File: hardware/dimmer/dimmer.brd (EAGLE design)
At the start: 112.1 x 40.6 mm, 34 parts, among them IC1 MEGA328PU, IC2 RFM12, IC3 7812L, IC4 LP2950Z, K1 G5LE, T1 BC547, T2 BC547, X1 AC In, X2 DIM Out, X3 AC Out

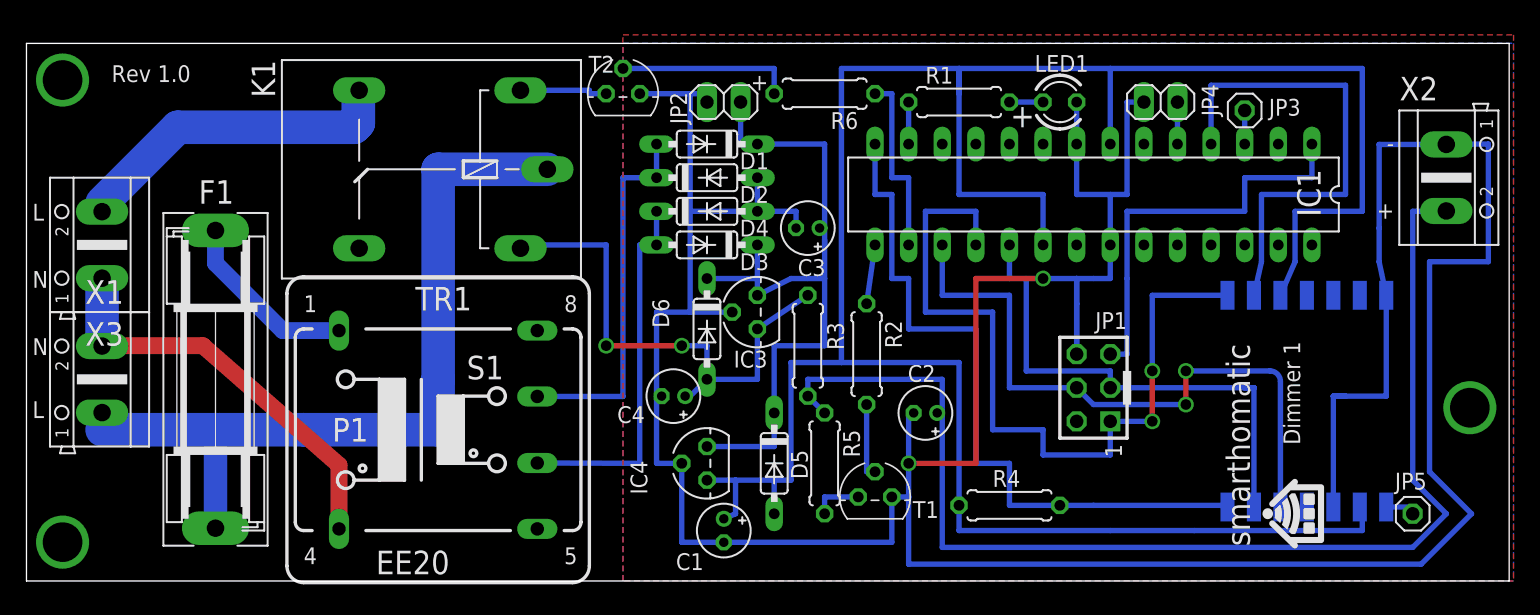
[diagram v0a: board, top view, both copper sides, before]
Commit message: Add 220nF capacitors at ATMega + RFM12. Use more powerful transformer, also 15V now. Use smaller relay. Use 15V transformer output voltage for relay instead of regulated voltage from 78L12. Smaller PCB.
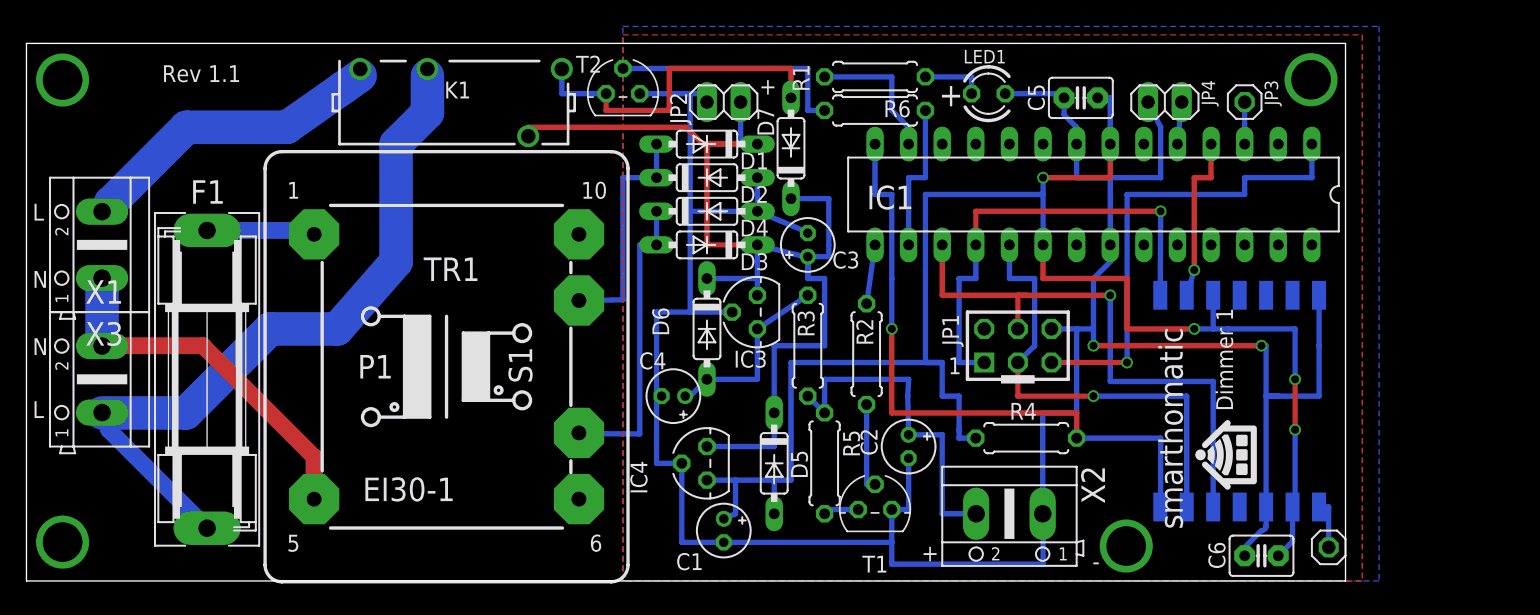
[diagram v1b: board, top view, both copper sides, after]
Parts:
- added C5, C6: 220n, capacitor-wima:C2.5-3
- added D7: 1N4148, diode:DO35-7
- K1: value G5LE -> G6D-1A-ASI12VDC; device relay:G5LE -> relay:G6D
- TR1: value 12V -> 15V; device trafo:EE20-1 -> trafo:EI30-1
- moved X2 41.7 mm to (68.6, 5.08), turned to 180 degrees
- moved JP5 6.84 mm to (92.7, 2.54)
- moved R1 6.63 mm to (58.4, 38.1)
- moved JP1 6.54 mm to (69.2, 17.8), turned to 0 degrees
- moved K1 5.68 mm to (26.7, 36.2), turned to 0 degrees
- moved LED1 5.43 mm to (67.0, 36.8)
- moved R4 5.24 mm to (69.8, 10.8)
- moved IC2 5.08 mm to (94.0, 21.6)
- moved TR1 4.80 mm to (26.0, 16.2)
- moved R6 4.02 mm to (58.4, 35.6)
- moved C2 2.84 mm to (61.0, 10.2), turned to 270 degrees
- moved C3 1.27 mm to (53.3, 25.4), turned to 90 degrees
- moved T1 0.95 mm to (58.4, 5.40)
- moved F1 0.63 mm to (7.94, 15.2)
- moved JP3 0.63 mm to (86.4, 36.2)
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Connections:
- removed net N$21: K1.S, X3.2
- new net N$20: K1.7, X3.2
- net GND: now also C5.2, C6.2
- net N$1: now also TR1.9; no longer TR1.7
- net N$10: no longer K1.2
- net N$18: now also D7.A
- net N$19: now also TR1.5; no longer TR1.4
- net N$22: now also K1.5; no longer K1.P
- net N$7: now also TR1.7; no longer TR1.6
- net N$9: now also D7.C, K1.13
- net VCC: now also C5.1, C6.1
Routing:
- net GND: track 277.2 -> 199.1 mm
- net N$17: track 91.9 -> 26.0 mm
- net VCC: track 190.4 -> 126.9 mm, vias 0 -> 4
- net N$9: track 55.4 -> 84.7 mm
- net N$21: track 25.0 -> 0.00 mm
- net N$4: track 59.7 -> 34.9 mm, vias 2 -> 1
- net N$10: track 38.9 -> 14.4 mm, vias 2 -> 0
- net N$15: track 36.9 -> 12.8 mm, vias 0 -> 1
- net N$20: track 0.00 -> 23.9 mm
- net N$18: track 6.73 -> 25.9 mm
- net N$1: track 28.1 -> 17.6 mm
- net N$22: track 62.2 -> 54.6 mm
- net N$6: track 3.17 -> 10.7 mm
- net N$5: track 41.1 -> 35.0 mm, vias 0 -> 1
- net N$3: track 49.2 -> 43.5 mm, vias 2 -> 1
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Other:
- board size 112.1 x 40.6 mm -> 99.7 x 40.6 mm
- board text added: "Rev 1.1"
- board text removed: "Rev 1.0"

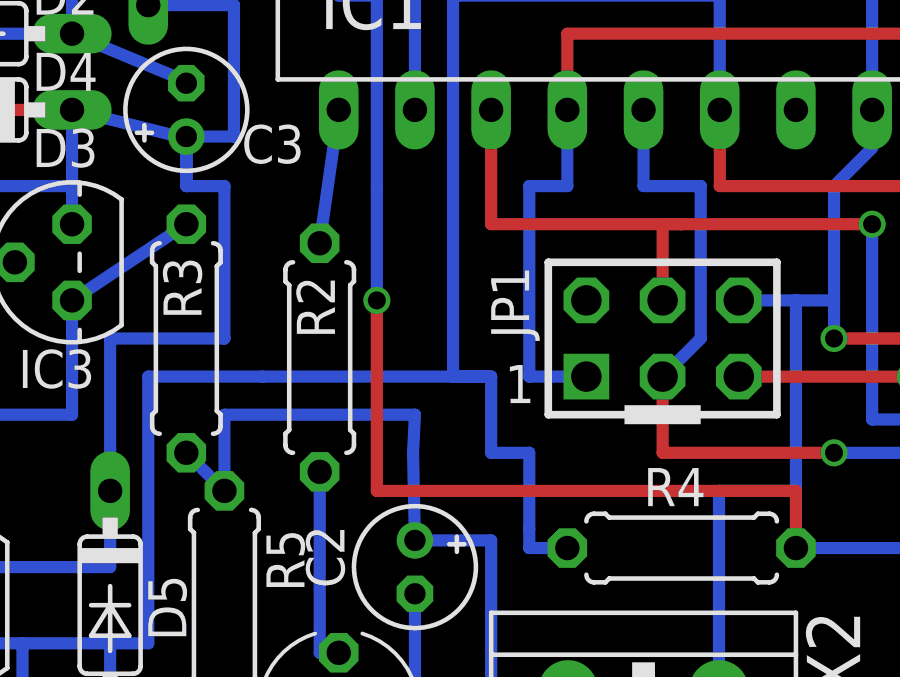
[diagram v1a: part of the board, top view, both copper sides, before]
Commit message: Add solder jumper for ISP VCC.
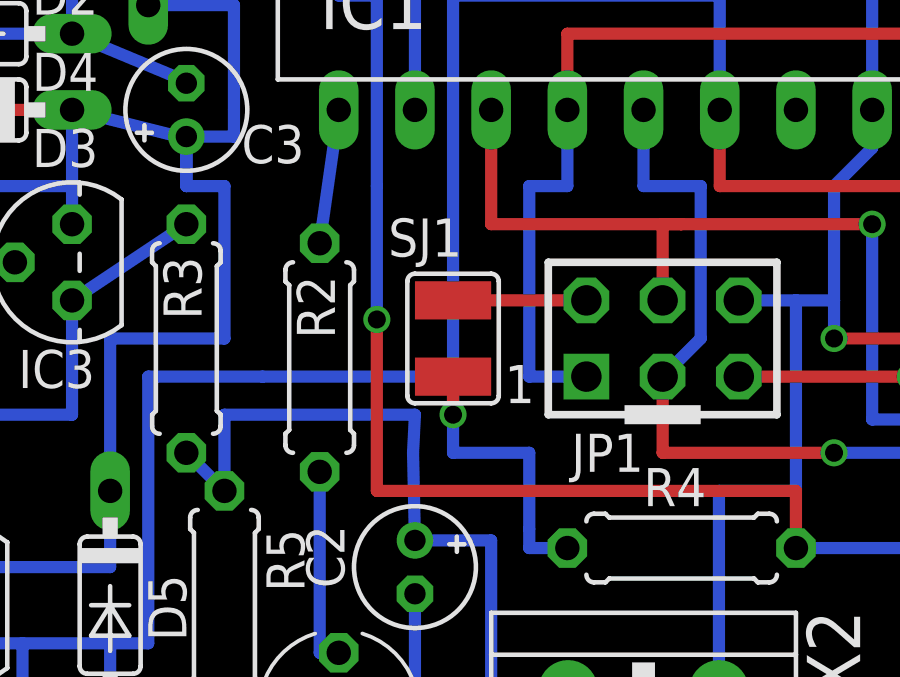
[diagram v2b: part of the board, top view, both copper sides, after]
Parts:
- added SJ1: ISP VCC, jumper:SJW
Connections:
- new net N$21: JP1.2, SJ1.1
- net VCC: now also SJ1.2
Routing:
- net N$21: track 0.00 -> 4.45 mm
- net VCC: track 126.9 -> 128.1 mm, vias 4 -> 5
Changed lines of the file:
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@@
 </element>
 <element name="JP1" library="avr-5-4.16" package="AVR-ISP-6" value="AVR-ISP-6" x="69.215" y="17.78" smashed="yes">
-<attribute name="NAME" x="64.77" y="17.78" size="1.27" layer="25" ratio="10" rot="R90"/>
+<attribute name="NAME" x="68.58" y="14.605" size="1.27" layer="25" ratio="10" rot="R180"/>
 <attribute name="VALUE" x="64.135" y="21.9075" size="1.27" layer="27" ratio="12"/>
 </element>
@@
 <attribute name="NAME" x="50.8" y="33.5915" size="1.27" layer="25" ratio="10" rot="R90"/>
 <attribute name="VALUE" x="54.737" y="27.8765" size="1.27" layer="27" ratio="10" rot="R90"/>
+</element>
+<element name="SJ1" library="jumper" package="SJW" value="ISP VCC" x="62.23" y="17.78" smashed="yes" rot="R270">
+<attribute name="NAME" x="60.071" y="20.5105" size="1.27" layer="25" ratio="10"/>
+<attribute name="VALUE" x="62.23" y="16.78" size="0.02" layer="27" rot="R270"/>
 </element>
 </elements>
@@
 <contactref element="C5" pad="1"/>
 <contactref element="C6" pad="1"/>
-<wire x1="55.88" y1="16.51" x2="63.5" y2="16.51" width="0.4064" layer="16"/>
-<wire x1="63.5" y1="16.51" x2="63.5" y2="13.97" width="0.4064" layer="16"/>
-<wire x1="63.5" y1="13.97" x2="64.77" y2="13.97" width="0.4064" layer="16"/>
+<wire x1="55.88" y1="16.51" x2="62.23" y2="16.51" width="0.4064" layer="16"/>
+<wire x1="62.23" y1="16.51" x2="62.23" y2="13.97" width="0.4064" layer="16"/>
+<wire x1="62.23" y1="13.97" x2="64.77" y2="13.97" width="0.4064" layer="16"/>
 <wire x1="64.77" y1="13.97" x2="64.77" y2="11.43" width="0.4064" layer="16"/>
 <wire x1="64.77" y1="11.43" x2="64.77" y2="10.795" width="0.4064" layer="16"/>
@@
 <wire x1="71.12" y1="30.48" x2="71.12" y2="29.21" width="0.4064" layer="16"/>
 <wire x1="71.12" y1="29.21" x2="71.12" y2="25.4" width="0.4064" layer="16"/>
-<wire x1="63.5" y1="16.51" x2="62.23" y2="16.51" width="0.4064" layer="16"/>
 <wire x1="62.23" y1="16.51" x2="62.23" y2="29.21" width="0.4064" layer="16"/>
 <wire x1="62.23" y1="29.21" x2="71.12" y2="29.21" width="0.4064" layer="16"/>
 <wire x1="75.2475" y1="36.5125" x2="76.2" y2="36.5125" width="0.4064" layer="16"/>
 <wire x1="76.2" y1="36.5125" x2="76.2" y2="33.02" width="0.4064" layer="16"/>
+<contactref element="SJ1" pad="2"/>
+<wire x1="62.23" y1="16.51" x2="62.23" y2="15.24" width="0.4064" layer="1"/>
+<via x="62.23" y="15.24" extent="1-16" drill="0.6" shape="square"/>
+<wire x1="62.23" y1="15.24" x2="62.23" y2="16.51" width="0.4064" layer="16"/>
 </signal>
 <signal name="N$3">
@@
 <wire x1="58.42" y1="29.21" x2="59.69" y2="29.21" width="0.4064" layer="16"/>
 <wire x1="59.69" y1="29.21" x2="59.69" y2="22.86" width="0.4064" layer="16"/>
-<wire x1="59.69" y1="22.86" x2="59.69" y2="19.05" width="0.4064" layer="16"/>
+<wire x1="59.69" y1="22.86" x2="59.69" y2="18.415" width="0.4064" layer="16"/>
 <wire x1="80.01" y1="10.795" x2="80.01" y2="5.715" width="0.4064" layer="16"/>
 <wire x1="80.01" y1="5.715" x2="80.01" y2="5.62" width="0.4064" layer="16"/>
 <wire x1="80.01" y1="5.62" x2="79.98" y2="5.59" width="0.4064" layer="16"/>
 <wire x1="73.66" y1="10.795" x2="80.01" y2="10.795" width="0.4064" layer="16"/>
-<via x="59.69" y="19.05" extent="1-16" drill="0.6" shape="square"/>
-<wire x1="59.69" y1="19.05" x2="59.69" y2="12.7" width="0.4064" layer="1"/>
+<via x="59.69" y="18.415" extent="1-16" drill="0.6" shape="square"/>
+<wire x1="59.69" y1="18.415" x2="59.69" y2="12.7" width="0.4064" layer="1"/>
 <wire x1="59.69" y1="12.7" x2="73.66" y2="12.7" width="0.4064" layer="1"/>
 <wire x1="73.66" y1="12.7" x2="73.66" y2="10.795" width="0.4064" layer="1"/>
@@
 <wire x1="19.51" y1="38.186775" x2="19.51" y2="38.695" width="1.27" layer="16"/>
 </signal>
+<signal name="N$21">
+<contactref element="JP1" pad="2"/>
+<contactref element="SJ1" pad="1"/>
+<wire x1="66.675" y1="19.05" x2="62.23" y2="19.05" width="0.4064" layer="1"/>
+</signal>
 </signals>

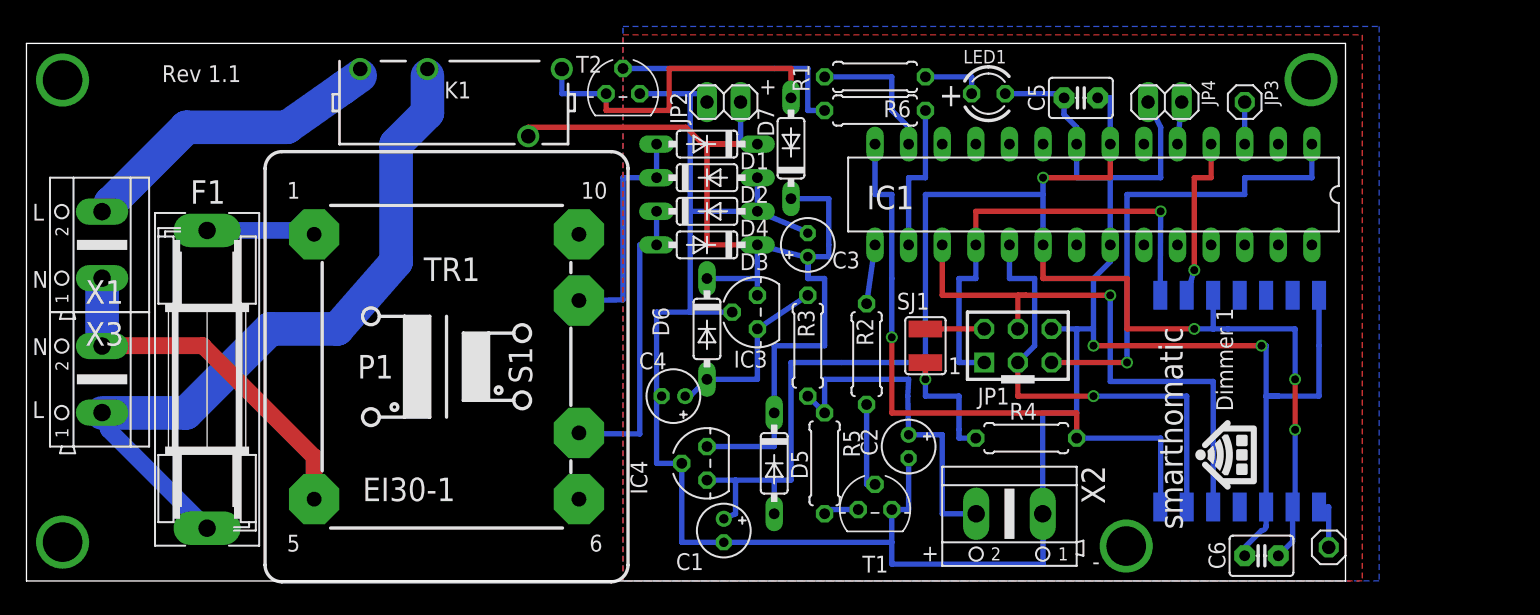
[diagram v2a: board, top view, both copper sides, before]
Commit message: Change SMD solder pad.
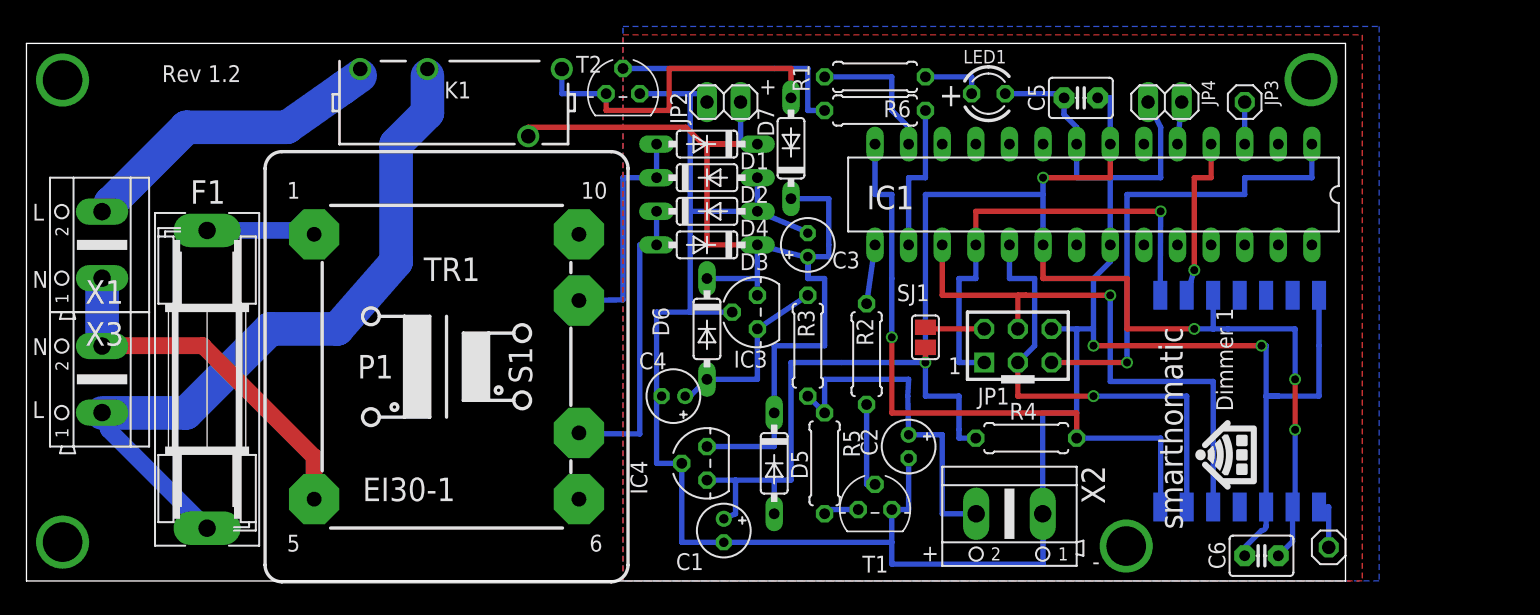
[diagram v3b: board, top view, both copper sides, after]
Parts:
- SJ1: device jumper:SJW -> jumper:SJ
- moved SJ1 0.63 mm to (62.2, 18.4)
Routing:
- net VCC: track 128.1 -> 126.7 mm
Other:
- board text added: "Rev 1.2"
- board text removed: "Rev 1.1"
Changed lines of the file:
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@@
 <text x="81.68021875" y="3.898665625" size="1.778" layer="25" font="vector" rot="R90">smarthomatic</text>
 <text x="85.476909375" y="12.837490625" size="1.27" layer="25" font="vector" rot="R90">Dimmer 1</text>
-<text x="4.5279" y="37.7094375" size="1.27" layer="25">Rev 1.1</text>
+<text x="4.5279" y="37.7094375" size="1.27" layer="25">Rev 1.2</text>
 <text x="65.0875" y="35.8775" size="1.778" layer="25" rot="MR0">+</text>
 <rectangle x1="87.237196875" y1="7.536375" x2="87.318196875" y2="7.54215625" layer="25" rot="R90"/>
@@
 <attribute name="VALUE" x="54.737" y="27.8765" size="1.27" layer="27" ratio="10" rot="R90"/>
 </element>
-<element name="SJ1" library="jumper" package="SJW" value="ISP VCC" x="62.23" y="17.78" smashed="yes" rot="R270">
-<attribute name="NAME" x="60.071" y="20.5105" size="1.27" layer="25" ratio="10"/>
-<attribute name="VALUE" x="62.23" y="16.78" size="0.02" layer="27" rot="R270"/>
+<element name="SJ1" library="jumper" package="SJ" value="ISP VCC" x="62.23" y="18.415" smashed="yes" rot="R270">
+<attribute name="NAME" x="60.071" y="21.1455" size="1.27" layer="25" ratio="10"/>
+<attribute name="VALUE" x="62.23" y="17.415" size="0.02" layer="27" rot="R270"/>
 </element>
 </elements>
@@
 <wire x1="76.2" y1="36.5125" x2="76.2" y2="33.02" width="0.4064" layer="16"/>
 <contactref element="SJ1" pad="2"/>
-<wire x1="62.23" y1="16.51" x2="62.23" y2="15.24" width="0.4064" layer="1"/>
-<via x="62.23" y="15.24" extent="1-16" drill="0.6" shape="square"/>
-<wire x1="62.23" y1="15.24" x2="62.23" y2="16.51" width="0.4064" layer="16"/>
+<wire x1="62.23" y1="17.653" x2="62.23" y2="16.51" width="0.4064" layer="1"/>
+<via x="62.23" y="16.51" extent="1-16" drill="0.6" shape="square"/>
 </signal>
 <signal name="N$3">
@@
 <contactref element="SJ1" pad="1"/>
 <wire x1="66.675" y1="19.05" x2="62.23" y2="19.05" width="0.4064" layer="1"/>
+<wire x1="62.23" y1="19.05" x2="62.23" y2="19.177" width="0.4064" layer="1"/>
 </signal>
 </signals>
